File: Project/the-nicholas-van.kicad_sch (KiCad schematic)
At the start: 38 parts, among them J1 JST SH, J2 Pico EZmate, J3 USB_C sink board 1.3mm, J4 Conn_01x05, SW1 BOOT0, U1 STM32F401CBUx, U2 XC6206PxxxMR, U3 74AHCT1G125, Y1 8 MHz

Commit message: created production files
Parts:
- C15, C16, C17, C18: value 100nF -> 100n

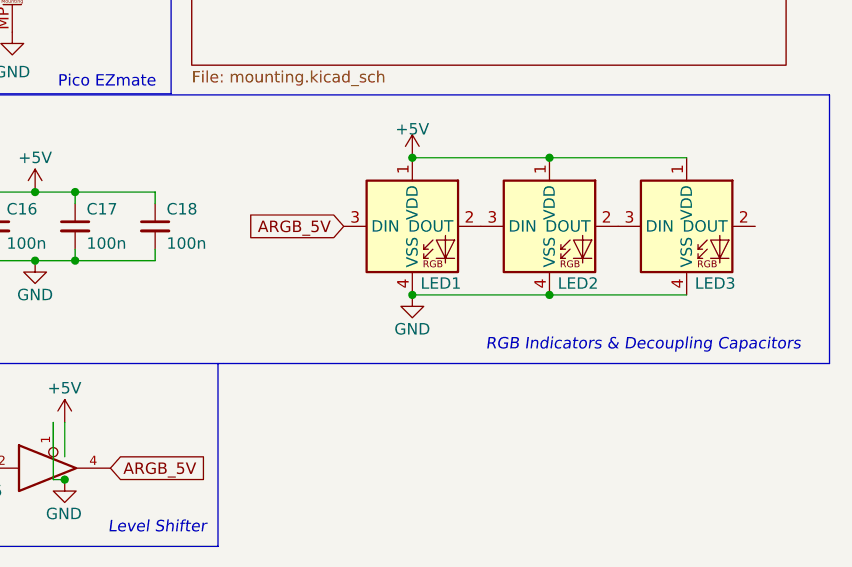
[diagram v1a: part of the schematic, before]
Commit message: added rgb breakout
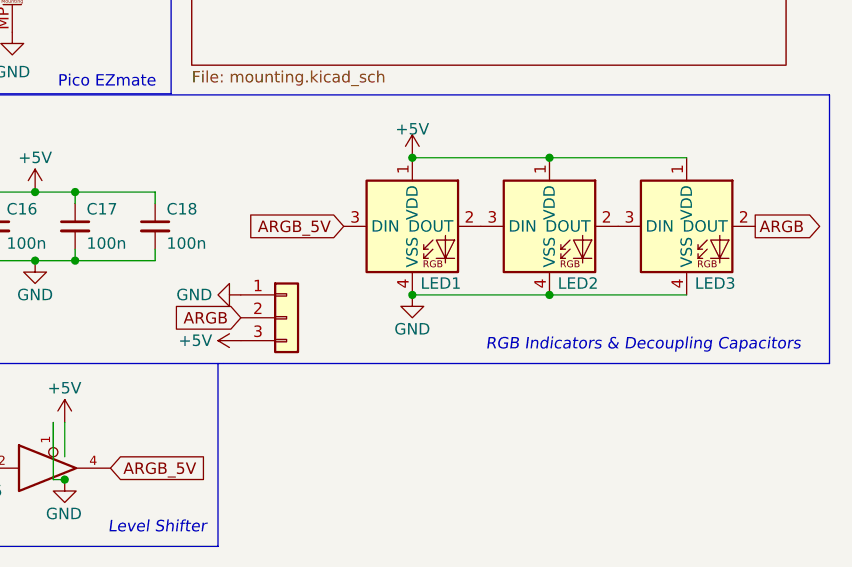
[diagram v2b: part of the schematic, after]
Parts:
- added J5: ARGB, Connector_PinHeader_1.27mm:PinHeader_1x03_P1.27mm_Vertical, symbol Connector_Generic:Conn_01x03
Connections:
- net +5V: now also J5.3 (Pin_3)
- net GND: now also J5.1 (Pin_1)
- net ARGB: now reaches LED3.2 (DOUT)
- net ARGB: now also J5.2 (Pin_2)
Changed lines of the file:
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@@
+    )
+  )
+  (global_label "ARGB" (shape input) (at 219.71 132.08 180) (fields_autoplaced)
+    (effects (font (size 1.27 1.27)) (justify right))
+    (property "Intersheetrefs" "${INTERSHEET_REFS}" (at 212.7186 132.08 0)
+      (effects (font (size 1.27 1.27)) (justify right) hide)
     )
   )
@@
     (effects (font (size 1.27 1.27)) (justify left))
     (property "Intersheetrefs" "${INTERSHEET_REFS}" (at 58.3406 13.0688 90)
+      (effects (font (size 1.27 1.27)) (justify left) hide)
+    )
+  )
+  (global_label "ARGB" (shape output) (at 276.86 121.92 0) (fields_autoplaced)
+    (effects (font (size 1.27 1.27)) (justify left))
+    (property "Intersheetrefs" "${INTERSHEET_REFS}" (at 284.6644 121.92 0)
       (effects (font (size 1.27 1.27)) (justify left) hide)
     )
@@
         (path "/690df46b-b605-4617-b545-6aaced86d0fc"
           (reference "#PWR0102") (unit 1)
+        )
+      )
+    )
+  )
+  (symbol (lib_id "Connector_Generic:Conn_01x03") (at 224.79 132.08 0) (unit 1)
+    (in_bom no) (on_board yes) (dnp no)
+    (property "Reference" "J5" (at 227.33 130.81 0)
+      (effects (font (size 1.27 1.27)) (justify left) hide)
+    )
+    (property "Value" "ARGB" (at 227.33 133.35 0)
+      (effects (font (size 1.27 1.27)) (justify left) hide)
+    )
+    (property "Footprint" "Connector_PinHeader_1.27mm:PinHeader_1x03_P1.27mm_Vertical" (at 224.79 132.08 0)
+      (effects (font (size 1.27 1.27)) hide)
+    )
+    (property "Datasheet" "~" (at 224.79 132.08 0)
+      (effects (font (size 1.27 1.27)) hide)
+    )
+    (pin "1")
+    (pin "2")
+    (pin "3")
+    (instances
+      (project "the-nicholas-van"
+        (path "/38f182bd-9097-4ce3-95d4-cd91b210c79b"
+          (reference "J5") (unit 1)
+        )
+      )
+      (project "Memoria"
+        (path "/ee27d19c-8dca-4ac8-a760-6dfd54d28071"
+          (reference "J1") (unit 1)
         )
       )
@@
     )
   )
+  (symbol (lib_id "power:+5V") (at 219.71 134.62 90) (unit 1)
+    (in_bom yes) (on_board yes) (dnp no)
+    (property "Reference" "#PWR053" (at 223.52 134.62 0)
+      (effects (font (size 1.27 1.27)) hide)
+    )
+    (property "Value" "+5V" (at 216.535 134.62 90)
+      (effects (font (size 1.27 1.27)) (justify left))
+    )
+    (property "Footprint" "" (at 219.71 134.62 0)
+      (effects (font (size 1.27 1.27)) hide)
+    )
+    (property "Datasheet" "" (at 219.71 134.62 0)
+      (effects (font (size 1.27 1.27)) hide)
+    )
+    (pin "1")
+    (instances
+      (project "the-nicholas-van"
+        (path "/38f182bd-9097-4ce3-95d4-cd91b210c79b"
+          (reference "#PWR053") (unit 1)
+        )
+      )
+      (project "Memoria"
+        (path "/ee27d19c-8dca-4ac8-a760-6dfd54d28071"
+          (reference "#PWR0111") (unit 1)
+        )
+      )
+    )
+  )
   (symbol (lib_id "power:GND") (at 50.8 120.65 0) (unit 1)
     (in_bom yes) (on_board yes) (dnp no)
@@
         )
       )
+    )
+  )
+  (symbol (lib_id "power:GND") (at 219.71 129.54 270) (unit 1)
+    (in_bom yes) (on_board yes) (dnp no)
+    (property "Reference" "#PWR052" (at 213.36 129.54 0)
+      (effects (font (size 1.27 1.27)) hide)
+    )
+    (property "Value" "GND" (at 216.535 129.54 90)
+      (effects (font (size 1.27 1.27)) (justify right))
+    )
+    (property "Footprint" "" (at 219.71 129.54 0)
+      (effects (font (size 1.27 1.27)) hide)
+    )
+    (property "Datasheet" "" (at 219.71 129.54 0)
+      (effects (font (size 1.27 1.27)) hide)
+    )
+    (pin "1")
+    (instances
+      (project "the-nicholas-van"
+        (path "/38f182bd-9097-4ce3-95d4-cd91b210c79b"
+          (reference "#PWR052") (unit 1)
+        )
+      )
+      (project "Memoria"
+        (path "/ee27d19c-8dca-4ac8-a760-6dfd54d28071"
+          (reference "#PWR0110") (unit 1)
+        )
+      )

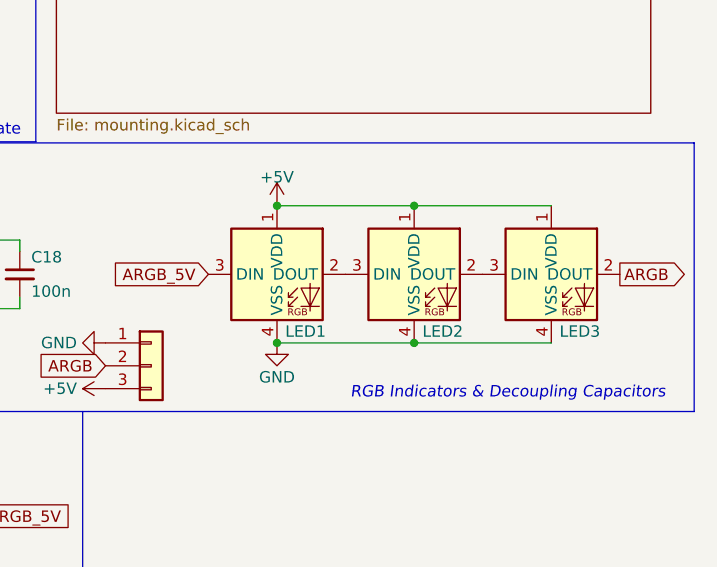
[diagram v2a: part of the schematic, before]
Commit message: rgb symbol/footprint mismatch corrected, fresh gerbers, etc
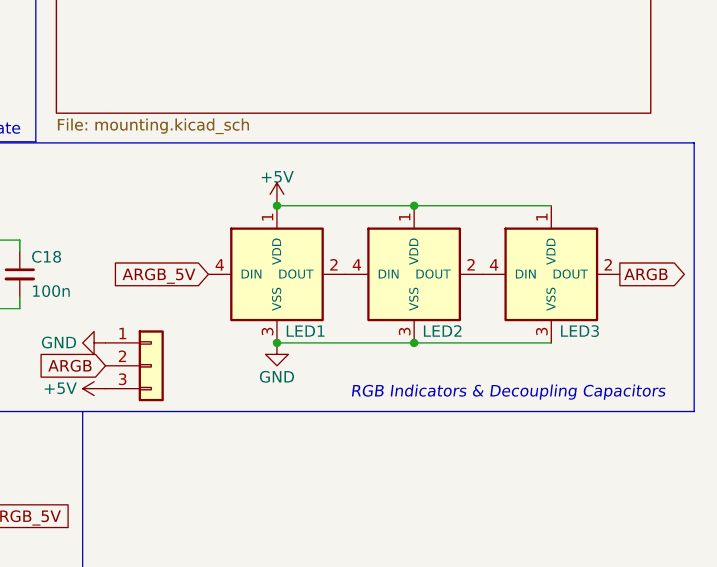
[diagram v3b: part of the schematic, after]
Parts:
- LED1, LED2, LED3: footprint PCM_marbastlib-various:LED_6028R -> cipulot_parts:SK6812-MINI-E; symbol marbastlib-various:SK6812MINI-E -> cipulot_parts:YS-SK6812MINI-E
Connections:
- net ARGB_5V: now also LED1.4 (DIN); no longer LED1.3 (DIN)
- net GND: now also LED1.3 (VSS), LED2.3 (VSS), LED3.3 (VSS); no longer LED1.4 (VSS), LED2.4 (VSS), LED3.4 (VSS)
- net at LED2.2 (DOUT): now also LED3.4 (DIN); no longer LED3.3 (DIN)
- net at LED1.2 (DOUT): now also LED2.4 (DIN); no longer LED2.3 (DIN)
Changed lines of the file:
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@@
     )
   )
-  (symbol (lib_id "marbastlib-various:SK6812MINI-E") (at 254 121.92 0) (unit 1)
+  (symbol (lib_id "cipulot_parts:YS-SK6812MINI-E") (at 254 121.92 0) (unit 1)
     (in_bom yes) (on_board yes) (dnp no)
     (property "Reference" "LED2" (at 257.175 128.27 0)
@@
       (effects (font (size 1.27 1.27)) hide)
     )
-    (property "Footprint" "PCM_marbastlib-various:LED_6028R" (at 254 121.92 0)
-      (effects (font (size 1.27 1.27)) hide)
-    )
-    (property "Datasheet" "" (at 254 121.92 0)
+    (property "Footprint" "cipulot_parts:SK6812-MINI-E" (at 256.54 128.27 0)
+      (effects (font (size 1.27 1.27)) hide)
+    )
+    (property "Datasheet" "" (at 256.54 128.27 0)
       (effects (font (size 1.27 1.27)) hide)
     )
@@
     )
   )
-  (symbol (lib_id "marbastlib-various:SK6812MINI-E") (at 238.76 121.92 0) (unit 1)
+  (symbol (lib_id "cipulot_parts:YS-SK6812MINI-E") (at 238.76 121.92 0) (unit 1)
     (in_bom yes) (on_board yes) (dnp no)
     (property "Reference" "LED1" (at 241.935 128.27 0)
@@
       (effects (font (size 1.27 1.27)) hide)
     )
-    (property "Footprint" "PCM_marbastlib-various:LED_6028R" (at 238.76 121.92 0)
-      (effects (font (size 1.27 1.27)) hide)
-    )
-    (property "Datasheet" "" (at 238.76 121.92 0)
+    (property "Footprint" "cipulot_parts:SK6812-MINI-E" (at 241.3 128.27 0)
+      (effects (font (size 1.27 1.27)) hide)
+    )
+    (property "Datasheet" "" (at 241.3 128.27 0)
       (effects (font (size 1.27 1.27)) hide)
     )
@@
     )
   )
-  (symbol (lib_id "marbastlib-various:SK6812MINI-E") (at 269.24 121.92 0) (unit 1)
+  (symbol (lib_id "cipulot_parts:YS-SK6812MINI-E") (at 269.24 121.92 0) (unit 1)
     (in_bom yes) (on_board yes) (dnp no)
     (property "Reference" "LED3" (at 272.415 128.27 0)
@@
       (effects (font (size 1.27 1.27)) hide)
     )
-    (property "Footprint" "PCM_marbastlib-various:LED_6028R" (at 269.24 121.92 0)
-      (effects (font (size 1.27 1.27)) hide)
-    )
-    (property "Datasheet" "" (at 269.24 121.92 0)
-      (effects (font (size 1.27 1.27)) hide)
-    )
+    (property "Footprint" "cipulot_parts:SK6812-MINI-E" (at 271.78 128.27 0)
+      (effects (font (size 1.27 1.27)) hide)
+    )
+    (property "Datasheet" "" (at 271.78 128.27 0)
+      (effects (font (size 1.27 1.27)) hide)
+    )

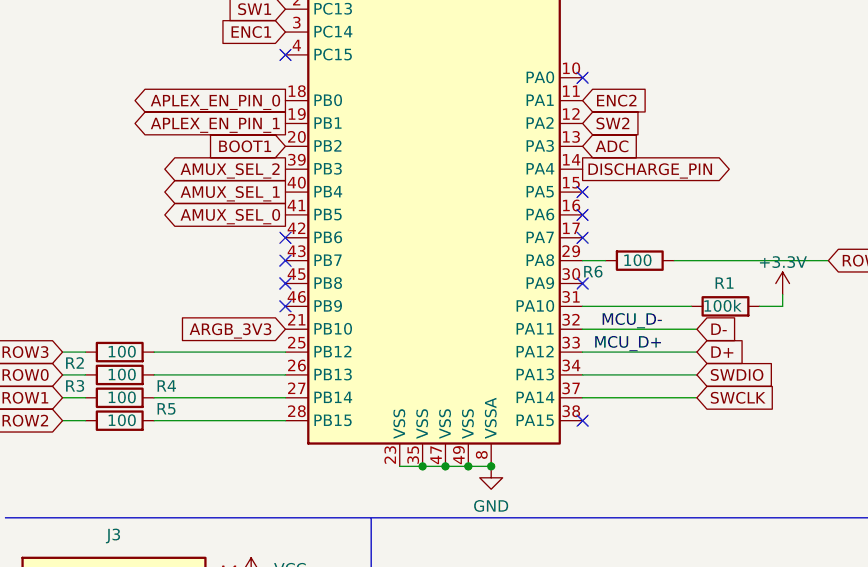
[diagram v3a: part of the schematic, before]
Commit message: changed rgb pin for better compatibilty
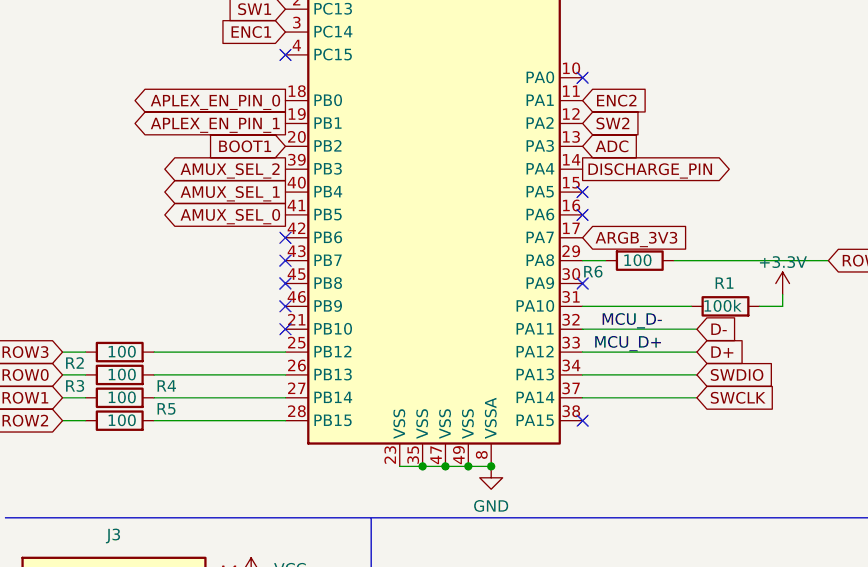
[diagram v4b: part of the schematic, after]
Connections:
- net ARGB_3V3: now also U1.17 (PA7); no longer U1.21 (PB10)
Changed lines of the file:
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@@
   (no_connect (at 43.18 81.28))
   (no_connect (at 39.37 144.78))
-  (no_connect (at 76.2 76.2))
+  (no_connect (at 43.18 86.36))
   (no_connect (at 43.18 76.2))
   (no_connect (at 76.2 96.52))
@@
     )
   )
-  (global_label "ARGB_3V3" (shape input) (at 43.18 86.36 180) (fields_autoplaced)
-    (effects (font (size 1.27 1.27)) (justify right))
-    (property "Intersheetrefs" "${INTERSHEET_REFS}" (at 43.18 88.1952 0)
-      (effects (font (size 1.27 1.27)) (justify right) hide)
-    )
-  )
+  (global_label "ARGB_3V3" (shape input) (at 76.2 76.2 0) (fields_autoplaced)
+    (effects (font (size 1.27 1.27)) (justify left))
+    (property "Intersheetrefs" "${INTERSHEET_REFS}" (at 88.4796 76.2 0)
+      (effects (font (size 1.27 1.27)) (justify left) hide)
+    )
+  )
